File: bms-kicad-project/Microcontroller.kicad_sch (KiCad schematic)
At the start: 38 parts, among them J2 12402012E212A, J3 DEBUG, J4 Conn_02x18_Odd_Even, J5 Conn_02x18_Odd_Even, Q14 BSS308PE_H6327, SW1 KMR223G LFG, SW2 KMR223G LFG, U4 W25Q128JVSIQ TR, U5 NCP1117ST33T3G, U6 RP2040, X1 ABM8-272-T3

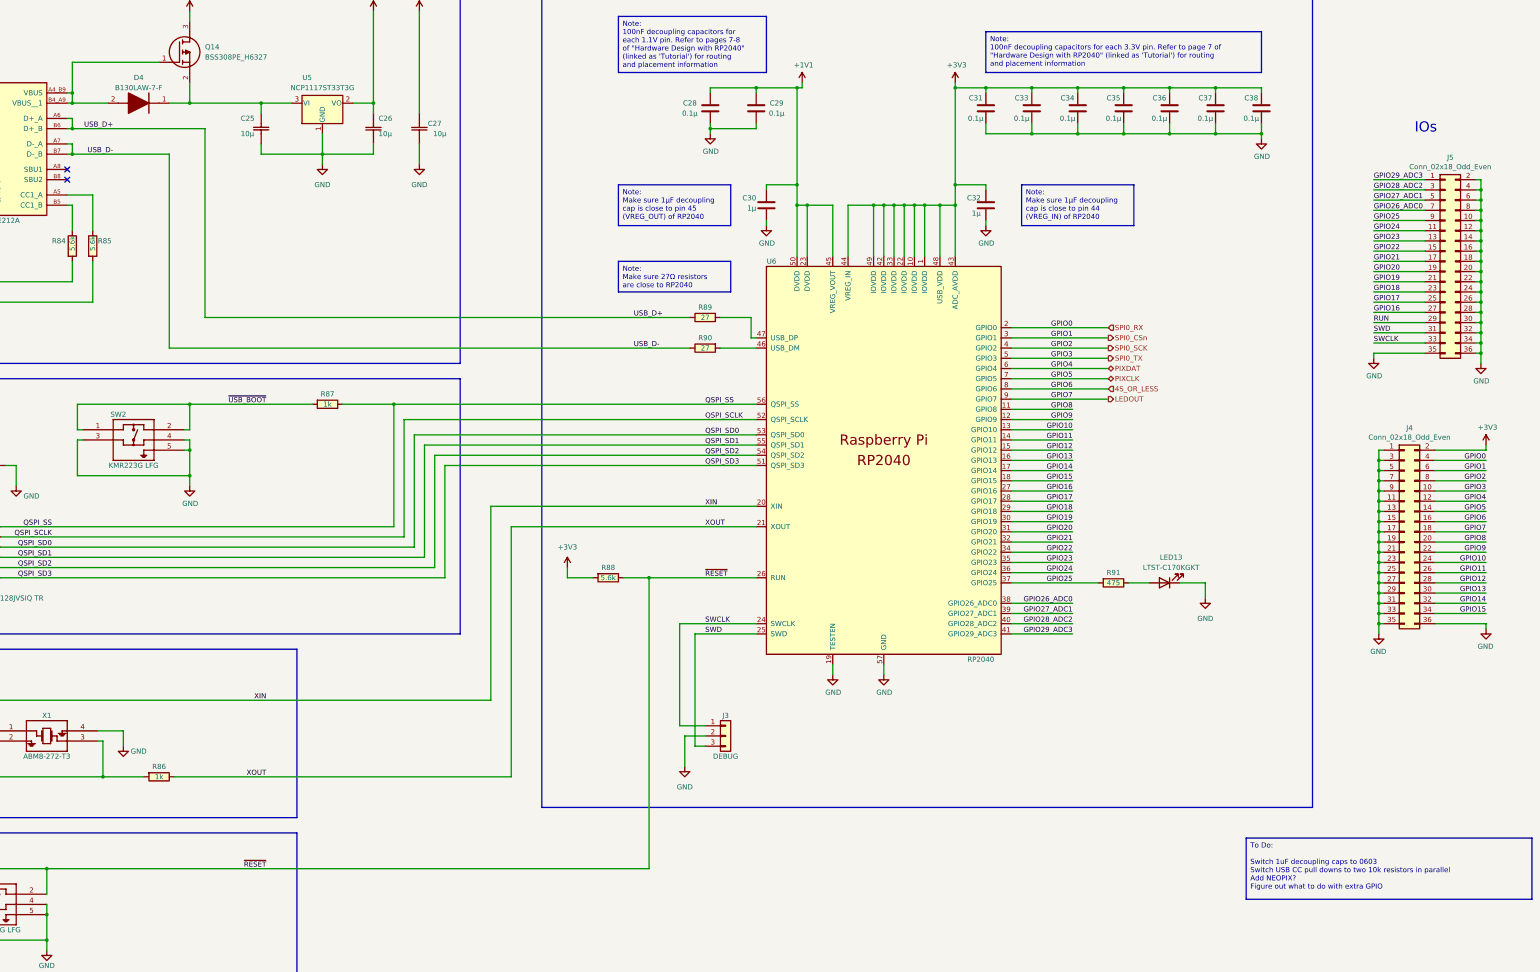
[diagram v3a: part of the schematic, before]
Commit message: feat: cell filtering/balancing switchover done
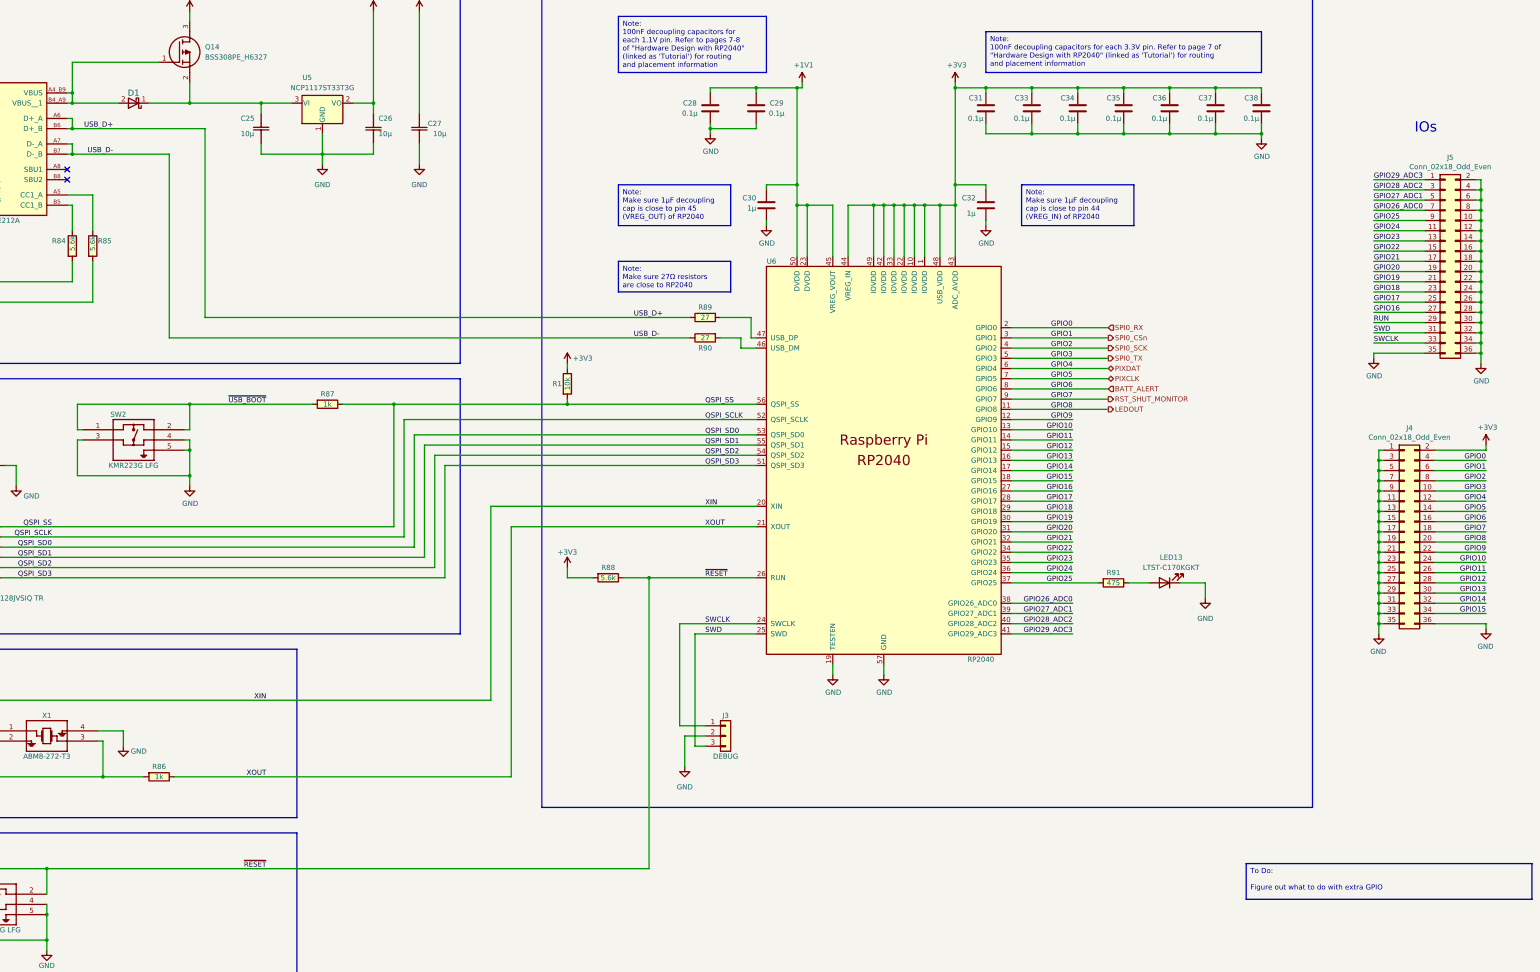
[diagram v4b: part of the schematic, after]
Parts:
- removed D4: B130LAW-7-F, FixedWing:SOD3716X145N, symbol FixedWing:B130LAW-7-F
- added D1: 100V, FixedWing:D_SOD-123, symbol FixedWing:BAS100AS_R1_00001
- added R1: 10k, FixedWing:KOA_Speer-RK73H2A-0-0-MFG, symbol FixedWing:RK73H2ATTD1002F
- C30, C32: footprint FixedWing:CAPC2012X140N -> FixedWing:CAPC1608X90N; symbol FixedWing:GCM21BR71C105KA58L -> FixedWing:GCM188R71C105KA64D; Manufacturer Part Number GCM21BR71C105KA58L -> GCM188R71C105KA64D
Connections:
- net GPIO8 is gone; now on net LEDOUT: J4.20 (Pin_20), U6.11 (GPIO8)
- net +3V3: now also R1.2
- net LEDOUT: no longer J4.18 (Pin_18), U6.9 (GPIO7)
- net QSPI_SS: now also R1.1
- net at J2.A4_B9 (VBUS), J2.B4_A9 (VBUS__1), Q14.1 (G): now also D1.2
- net at C25.1, Q14.2 (S), U5.3 (VI): now also D1.1
- net 4S_OR_LESS renamed BATT_ALERT
- new net RST_SHUT_MONITOR: J4.18 (Pin_18), U6.9 (GPIO7)
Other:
- moved on the sheet: R90

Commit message: feat: don't even know what I changed, just zoned out for several hours. Made PCB r/a mount XT-60s and solder pads into a 2-for-1 deal
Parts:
- renumbered C22 to C23, C23 to C24, C24 to C25, C25 to C26, C26 to C27, C27 to C28, C28 to C29, C29 to C30, C30 to C31, C31 to C32, C32 to C33, C33 to C34, C34 to C35, C35 to C36, C36 to C37, C37 to C38, C38 to C39, D1 to D2, Q14 to Q13, R88 to R100, R89 to R101, R90 to R102, R91 to R103, R84 to R95, R85 to R96, R86 to R97, R87 to R98, R1 to R99, U4 to U3, U5 to U4, U6 to U5
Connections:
- net LEDOUT renamed RGB_DIN

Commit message: feat: schematic pretty much done
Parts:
- removed J4, J5: Conn_02x18_Odd_Even, Connector_PinHeader_2.54mm:PinHeader_2x18_P2.54mm_Vertical, symbol Connector_Generic:Conn_02x18_Odd_Even
- removed R100: 5.6k, FixedWing:RESC2012X60N, symbol FixedWing:RK73H2ATTD5601F
- added J5: Conn_02x20_Counter_Clockwise, Connector_PinHeader_2.54mm:PinHeader_2x20_P2.54mm_Vertical, symbol Connector_Generic:Conn_02x20_Counter_Clockwise
- added R100: 10k, FixedWing:KOA_Speer-RK73H2A-0-0-MFG, symbol FixedWing:RK73H2ATTD1002F
- added TP10, TP11, TP12, TP13, TP14, TP15, TP5, TP6, TP7, TP8, TP9: TestPoint, TestPoint:TestPoint_Pad_D1.5mm, symbol Connector:TestPoint
- renumbered C34 to C33, C35 to C34, C36 to C35, C33 to C36, J2 to J3, J3 to J4
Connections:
- net ~{RESET} is gone; now on net RUN: SW1.1, SW1.2, U5.26 (RUN)
- net +1V1: now also TP14.1
- net +3V3: now also R100.1, TP15.1
- net +5V: now also J5.40 (Pin_40)
- net BATT_ALERT: now also J5.9 (Pin_9)
- net GND: now also U3.4 (GND), J5.13 (Pin_13), J5.18 (Pin_18), J5.23 (Pin_23), J5.28 (Pin_28), J5.3 (Pin_3), J5.33 (Pin_33), J5.8 (Pin_8)
- net GPIO10: now also J5.14 (Pin_14)
- net GPIO11: now also J5.15 (Pin_15)
- net GPIO12: now also J5.16 (Pin_16)
- net GPIO13: now also J5.17 (Pin_17)
- net GPIO14: now also J5.19 (Pin_19)
- net GPIO15: now also J5.20 (Pin_20)
- net GPIO16: now also J5.21 (Pin_21)
- net GPIO17: now also J5.22 (Pin_22)
- net GPIO18: now also J5.24 (Pin_24)
- net GPIO19: now also J5.25 (Pin_25)
- net GPIO20: now also J5.26 (Pin_26)
- net GPIO21: now also J5.27 (Pin_27)
- net GPIO22: now also J5.29 (Pin_29)
- net GPIO23: now also J5.31 (Pin_31)
- net GPIO24: now also J5.32 (Pin_32)
- net GPIO25: now also J5.34 (Pin_34)
- net GPIO26_ADC0: now also J5.35 (Pin_35)
- net GPIO27_ADC1: now also J5.36 (Pin_36)
- net GPIO28_ADC2: now also J5.37 (Pin_37)
- net GPIO29_ADC3: now also J5.38 (Pin_38)
- net GPIO9: now also J5.12 (Pin_12)
- net PIXCLK: now also J5.7 (Pin_7)
- net PIXDAT: now also J5.6 (Pin_6)
- net QSPI_SCLK: now also TP7.1
- net QSPI_SD0: now also TP9.1
- net QSPI_SD1: now also TP10.1
- net QSPI_SD2: now also TP11.1
- net QSPI_SD3: now also TP12.1
- net QSPI_SS: now also TP6.1
- net RGB_DIN: now also J5.11 (Pin_11)
- net RST_SHUT_MONITOR: now also J5.10 (Pin_10)
- net RUN: now also J5.30 (Pin_30), R100.2, TP13.1
- net SPI0_CSn: now also J5.2 (Pin_2)
- net SPI0_RX: now also J5.1 (Pin_1)
- net SPI0_SCK: now also J5.4 (Pin_4)
- net SPI0_TX: now also J5.5 (Pin_5)
- net at D2.2, J3.A4_B9 (VBUS), J3.B4_A9 (VBUS__1)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: now also TP5.1
- net at C26.1, D2.1, Q13.2 (S)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: now also TP8.1
- new net +3.3V: J5.39 (Pin_39)
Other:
- note added: "- Adafruit Feather RP2040"
- note added: "- Minimal design example by Raspberry Pi"
- note added: "- Raspberry Pi Pico"
- moved on the sheet: C26, C27, C28, C29, C30, C32, C33, C34, C35, C36, C37, C38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

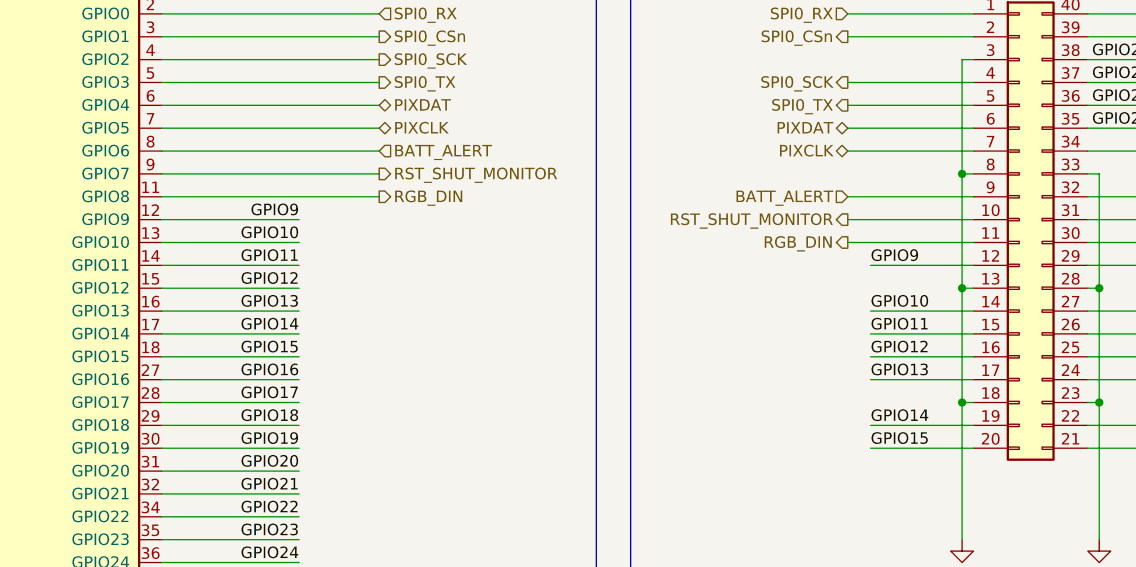
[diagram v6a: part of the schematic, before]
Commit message: feat: added current sense DAC
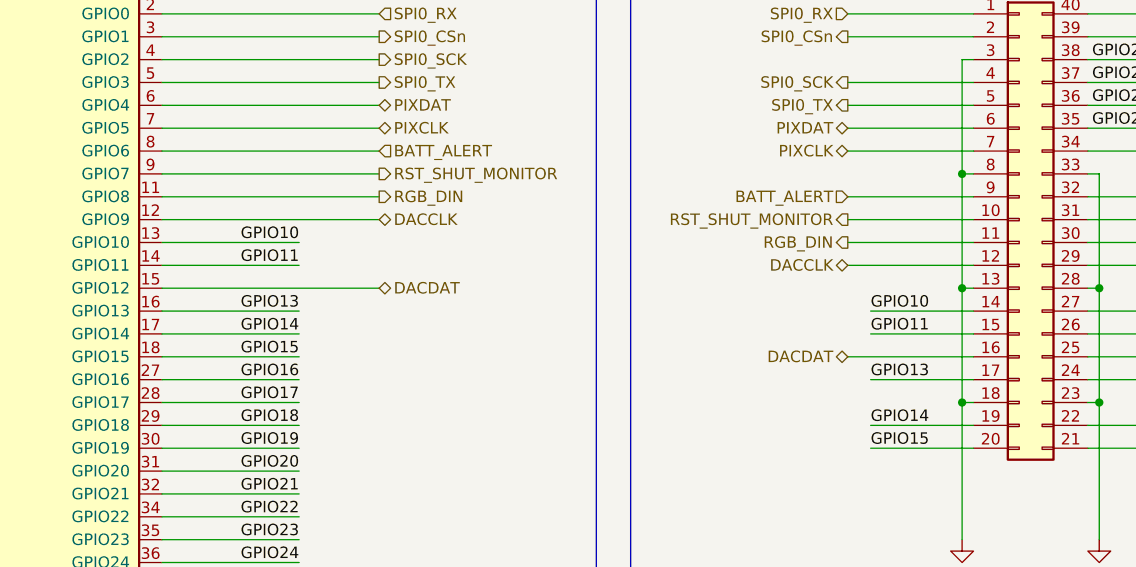
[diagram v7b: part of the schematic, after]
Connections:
- net GPIO12 renamed DACDAT
- net GPIO9 renamed DACCLK
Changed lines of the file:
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@@
     (stroke (width 0) (type default))
   )
-  (wire (pts (xy 367.03 140.97) (xy 378.46 140.97))
+  (wire (pts (xy 364.49 140.97) (xy 378.46 140.97))
     (stroke (width 0) (type default))
   )
@@
     (stroke (width 0) (type default))
   )
-  (wire (pts (xy 288.29 125.73) (xy 303.53 125.73))
+  (wire (pts (xy 288.29 125.73) (xy 312.42 125.73))
     (stroke (width 0) (type default))
   )
@@
     (stroke (width 0) (type default))
   )
-  (wire (pts (xy 288.29 133.35) (xy 303.53 133.35))
+  (wire (pts (xy 288.29 133.35) (xy 312.42 133.35))
     (stroke (width 0) (type default))
   )
@@
     (stroke (width 0) (type default))
   )
-  (wire (pts (xy 367.03 130.81) (xy 378.46 130.81))
+  (wire (pts (xy 364.49 130.81) (xy 378.46 130.81))
     (stroke (width 0) (type default))
   )
@@
     (effects (font (size 1.27 1.27)) (justify left bottom))
   )
-  (label "GPIO12" (at 367.03 140.97 0) (fields_autoplaced)
-    (effects (font (size 1.27 1.27)) (justify left bottom))
-  )
   (label "GPIO20" (at 303.53 153.67 180) (fields_autoplaced)
     (effects (font (size 1.27 1.27)) (justify right bottom))
@@
     (effects (font (size 1.27 1.27)) (justify left bottom))
   )
-  (label "GPIO9" (at 367.03 130.81 0) (fields_autoplaced)
-    (effects (font (size 1.27 1.27)) (justify left bottom))
-  )
   (label "QSPI_SD0" (at 212.09 129.54 0) (fields_autoplaced)
     (effects (font (size 1.27 1.27)) (justify left bottom))
@@
     (effects (font (size 1.27 1.27)) (justify right bottom))
   )
-  (label "GPIO9" (at 303.53 125.73 180) (fields_autoplaced)
-    (effects (font (size 1.27 1.27)) (justify right bottom))
-  )
   (label "GPIO15" (at 303.53 140.97 180) (fields_autoplaced)
-    (effects (font (size 1.27 1.27)) (justify right bottom))
-  )
-  (label "GPIO12" (at 303.53 133.35 180) (fields_autoplaced)
     (effects (font (size 1.27 1.27)) (justify right bottom))
   )
@@
     (effects (font (size 1.27 1.27)) (justify left))
   )
+  (hierarchical_label "DACCLK" (shape bidirectional) (at 364.49 130.81 180) (fields_autoplaced)
+    (effects (font (size 1.27 1.27)) (justify right))
+  )
+  (hierarchical_label "DACDAT" (shape bidirectional) (at 312.42 133.35 0) (fields_autoplaced)
+    (effects (font (size 1.27 1.27)) (justify left))
+  )
   (hierarchical_label "PIXDAT" (shape bidirectional) (at 312.42 113.03 0) (fields_autoplaced)
     (effects (font (size 1.27 1.27)) (justify left))
@@
     (effects (font (size 1.27 1.27)) (justify right))
   )
+  (hierarchical_label "DACCLK" (shape bidirectional) (at 312.42 125.73 0) (fields_autoplaced)
+    (effects (font (size 1.27 1.27)) (justify left))
+  )
+  (hierarchical_label "DACDAT" (shape bidirectional) (at 364.49 140.97 180) (fields_autoplaced)
+    (effects (font (size 1.27 1.27)) (justify right))
+  )
